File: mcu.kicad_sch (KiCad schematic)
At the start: 0 parts

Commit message: add mcu, sensor, sensor inst, power
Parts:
- added C7: 100n, Capacitor_SMD:C_0805_2012Metric, symbol Device:C
- added H1, H2, H3: MountingHole, MountingHole:MountingHole_3mm, symbol Mechanical:MountingHole
- added Q1, Q2: S8050, Package_TO_SOT_SMD:SOT-23, symbol Transistor_BJT:S8050
- added R8, R9: 12k, Resistor_SMD:R_0805_2012Metric, symbol Device:R
- added U4: ESP32-WROOM-32U, RF_Module:ESP32-WROOM-32U, symbol RF_Module:ESP32-WROOM-32U
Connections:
- new net: Q1.2 (B), R8.2
- new net: Q2.2 (B), R9.2
- new net 3V3: C7.1, U4.2 (VDD)
- new net DTR: Q2.1 (E), R8.1
- new net EN: Q1.3 (C), U4.3 (EN)
- new net GND: C7.2, U4.1 (GND), U4.15 (GND), U4.38 (GND), U4.39 (GND)
- new net IO0: Q2.3 (C), U4.25 (IO0)
- new net RDY: U4.24 (IO2)
- new net RTS: Q1.1 (E), R9.1
- new net RXD: U4.34 (RXD0/IO3)
- new net SCL: U4.36 (IO22)
- new net SDA: U4.33 (IO21)
- new net TXD: U4.35 (TXD0/IO1)

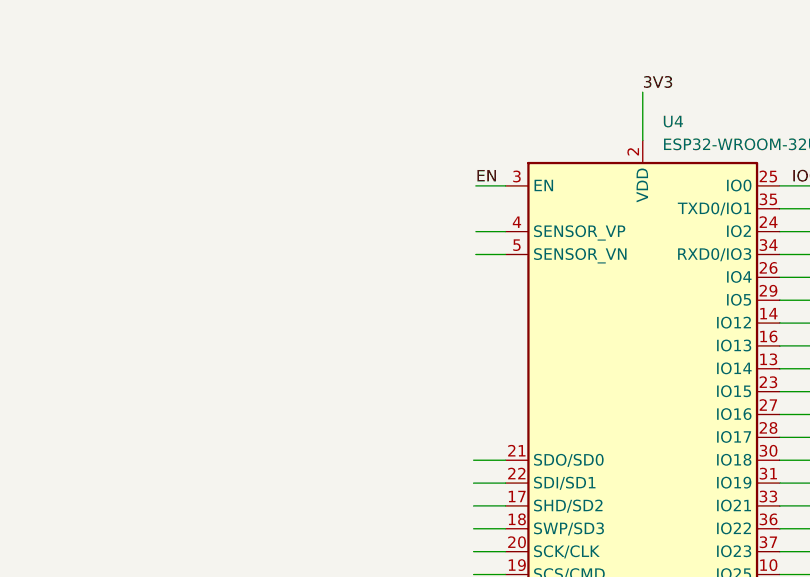
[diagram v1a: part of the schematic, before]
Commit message: add reset button
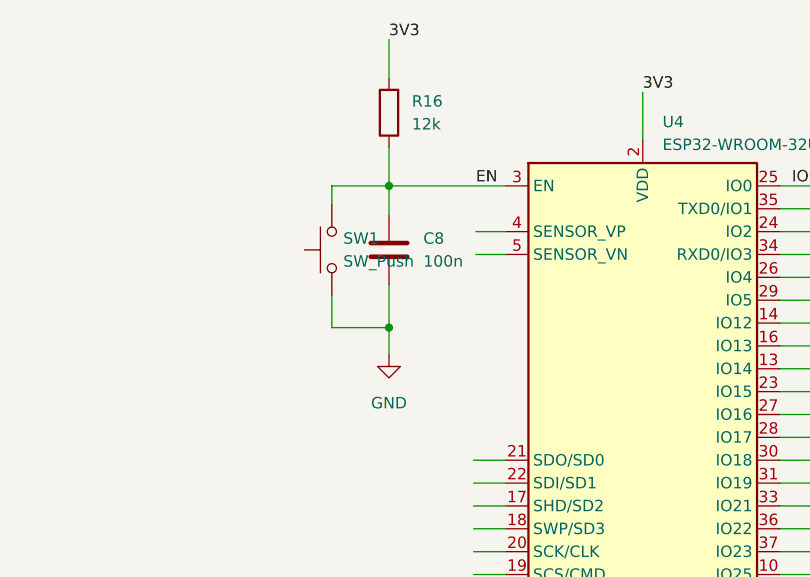
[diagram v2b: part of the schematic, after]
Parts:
- added C8: 100n, Capacitor_SMD:C_0805_2012Metric, symbol Device:C
- added R16: 12k, Resistor_SMD:R_0805_2012Metric, symbol Device:R
- added SW1: SW_Push, symbol Switch:SW_Push
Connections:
- net 3V3: now also R16.2
- net EN: now also C8.1, R16.1, SW1.2
- net GND: now also C8.2, SW1.1
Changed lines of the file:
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@@
   (junction (at 43.18 138.43) (diameter 0) (color 0 0 0 0)
   )
+  (junction (at 113.03 47.498) (diameter 0) (color 0 0 0 0)
+  )
+  (junction (at 113.03 63.246) (diameter 0) (color 0 0 0 0)
+  )
   (junction (at 41.656 155.448) (diameter 0) (color 0 0 0 0)
   )
@@
     (stroke (width 0) (type default))
   )
+  (wire (pts (xy 113.03 47.498) (xy 113.03 50.8))
+    (stroke (width 0) (type default))
+  )
   (wire (pts (xy 156.464 80.518) (xy 160.782 80.518))
     (stroke (width 0) (type default))
@@
     (stroke (width 0) (type default))
   )
+  (wire (pts (xy 113.03 63.246) (xy 113.03 58.42))
+    (stroke (width 0) (type default))
+  )
+  (wire (pts (xy 106.68 63.246) (xy 113.03 63.246))
+    (stroke (width 0) (type default))
+  )
   (wire (pts (xy 156.464 98.298) (xy 160.782 98.298))
     (stroke (width 0) (type default))
@@
     (stroke (width 0) (type default))
   )
+  (wire (pts (xy 113.03 31.242) (xy 113.03 35.56))
+    (stroke (width 0) (type default))
+  )
   (wire (pts (xy 156.464 103.378) (xy 160.782 103.378))
     (stroke (width 0) (type default))
@@
     (stroke (width 0) (type default))
   )
+  (wire (pts (xy 106.68 47.498) (xy 113.03 47.498))
+    (stroke (width 0) (type default))
+  )
   (wire (pts (xy 156.464 67.818) (xy 160.782 67.818))
     (stroke (width 0) (type default))
   )
-  (wire (pts (xy 122.682 47.498) (xy 125.984 47.498))
+  (wire (pts (xy 113.03 47.498) (xy 125.984 47.498))
     (stroke (width 0) (type default))
   )
@@
     (stroke (width 0) (type default))
   )
+  (wire (pts (xy 113.03 63.246) (xy 113.03 66.294))
+    (stroke (width 0) (type default))
+  )
   (wire (pts (xy 141.224 113.538) (xy 141.224 115.824))
     (stroke (width 0) (type default))
@@
     (stroke (width 0) (type default))
   )
+  (wire (pts (xy 113.03 43.18) (xy 113.03 47.498))
+    (stroke (width 0) (type default))
+  )
+  (wire (pts (xy 106.68 59.69) (xy 106.68 63.246))
+    (stroke (width 0) (type default))
+  )
   (wire (pts (xy 43.18 138.43) (xy 43.18 148.336))
+    (stroke (width 0) (type default))
+  )
+  (wire (pts (xy 106.68 49.53) (xy 106.68 47.498))
     (stroke (width 0) (type default))
   )
@@
   (label "IO0" (at 160.782 47.498 180) (fields_autoplaced)
     (effects (font (size 1.27 1.27)) (justify right bottom))
+  )
+  (label "3V3" (at 113.03 31.242 0) (fields_autoplaced)
+    (effects (font (size 1.27 1.27)) (justify left bottom))
   )
   (label "3V3" (at 59.69 56.896 0) (fields_autoplaced)
@@
         (path "/8f227bf3-f4cf-485c-a746-8377af835d89/10be11e8-d58f-4934-80aa-7bf19d703461"
           (reference "H1") (unit 1)
+        )
+      )
+    )
+  )
+  (symbol (lib_id "power:GND") (at 113.03 66.294 0) (unit 1)
+    (in_bom yes) (on_board yes) (dnp no) (fields_autoplaced)
+    (property "Reference" "#PWR029" (at 113.03 72.644 0)
+      (effects (font (size 1.27 1.27)) hide)
+    )
+    (property "Value" "GND" (at 113.03 71.628 0)
+      (effects (font (size 1.27 1.27)))
+    )
+    (property "Footprint" "" (at 113.03 66.294 0)
+      (effects (font (size 1.27 1.27)) hide)
+    )
+    (property "Datasheet" "" (at 113.03 66.294 0)
+      (effects (font (size 1.27 1.27)) hide)
+    )
+    (pin "1")
+    (instances
+      (project "scale"
+        (path "/8f227bf3-f4cf-485c-a746-8377af835d89/10be11e8-d58f-4934-80aa-7bf19d703461"
+          (reference "#PWR029") (unit 1)
+        )
+      )
+    )
+  )
+  (symbol (lib_id "Device:C") (at 113.03 54.61 0) (unit 1)
+    (in_bom yes) (on_board yes) (dnp no) (fields_autoplaced)
+    (property "Reference" "C8" (at 116.84 53.34 0)
+      (effects (font (size 1.27 1.27)) (justify left))
+    )
+    (property "Value" "100n" (at 116.84 55.88 0)
+      (effects (font (size 1.27 1.27)) (justify left))
+    )
+    (property "Footprint" "Capacitor_SMD:C_0805_2012Metric" (at 113.9952 58.42 0)
+      (effects (font (size 1.27 1.27)) hide)
+    )
+    (property "Datasheet" "~" (at 113.03 54.61 0)
+      (effects (font (size 1.27 1.27)) hide)
+    )
+    (pin "1")
+    (pin "2")
+    (instances
+      (project "scale"
+        (path "/8f227bf3-f4cf-485c-a746-8377af835d89/10be11e8-d58f-4934-80aa-7bf19d703461"
+          (reference "C8") (unit 1)
+        )
+      )
+    )
+  )
+  (symbol (lib_id "Switch:SW_Push") (at 106.68 54.61 90) (unit 1)
+    (in_bom yes) (on_board yes) (dnp no) (fields_autoplaced)
+    (property "Reference" "SW1" (at 107.95 53.34 90)
+      (effects (font (size 1.27 1.27)) (justify right))
+    )
+    (property "Value" "SW_Push" (at 107.95 55.88 90)
+      (effects (font (size 1.27 1.27)) (justify right))
+    )
+    (property "Footprint" "" (at 101.6 54.61 0)
+      (effects (font (size 1.27 1.27)) hide)
+    )
+    (property "Datasheet" "~" (at 101.6 54.61 0)
+      (effects (font (size 1.27 1.27)) hide)
+    )
+    (pin "1")
+    (pin "2")
+    (instances
+      (project "scale"
+        (path "/8f227bf3-f4cf-485c-a746-8377af835d89/10be11e8-d58f-4934-80aa-7bf19d703461"
+          (reference "SW1") (unit 1)
         )
       )
@@
         )
       )
+    )
+  )
+  (symbol (lib_id "Device:R") (at 113.03 39.37 180) (unit 1)
+    (in_bom yes) (on_board yes) (dnp no) (fields_autoplaced)
+    (property "Reference" "R16" (at 115.57 38.1 0)
+      (effects (font (size 1.27 1.27)) (justify right))
+    )
+    (property "Value" "12k" (at 115.57 40.64 0)
+      (effects (font (size 1.27 1.27)) (justify right))
+    )
+    (property "Footprint" "Resistor_SMD:R_0805_2012Metric" (at 114.808 39.37 90)
+      (effects (font (size 1.27 1.27)) hide)
+    )
+    (property "Datasheet" "~" (at 113.03 39.37 0)
+      (effects (font (size 1.27 1.27)) hide)
+    )
+    (pin "1")
+    (pin "2")
+    (instances
+      (project "scale"
+        (path "/8f227bf3-f4cf-485c-a746-8377af835d89/10be11e8-d58f-4934-80aa-7bf19d703461"
+          (reference "R16") (unit 1)
+        )
+      )

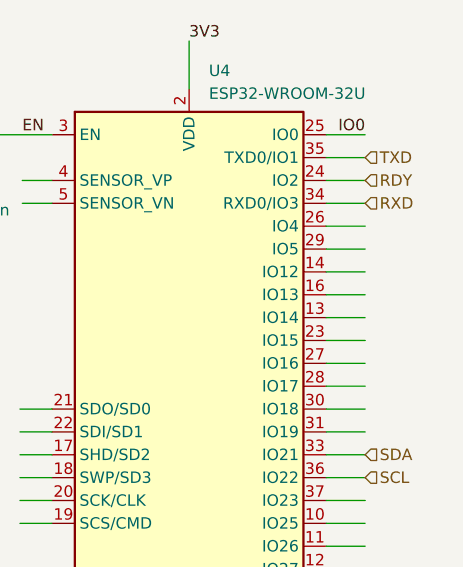
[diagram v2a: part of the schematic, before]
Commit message: add footprint and step
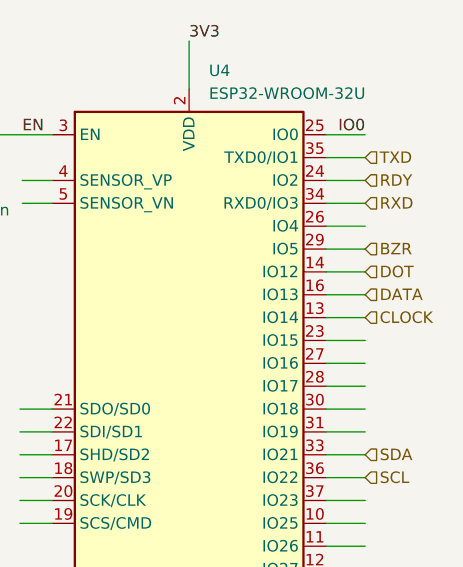
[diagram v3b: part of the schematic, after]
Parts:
- SW1: footprint (none) -> Button_Switch_SMD:SW_DIP_SPSTx01_Slide_6.7x4.1mm_W6.73mm_P2.54mm_LowProfile_JPin
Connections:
- net CLOCK: now reaches U4.13 (IO14)
- net DOT: now reaches U4.14 (IO12)
- net DATA: now reaches U4.16 (IO13)
- net BZR: now reaches U4.29 (IO5)
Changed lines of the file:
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@@
     (effects (font (size 1.27 1.27)) (justify right))
+  )
+  (hierarchical_label "CLOCK" (shape input) (at 160.782 67.818 0) (fields_autoplaced)
+    (effects (font (size 1.27 1.27)) (justify left))
   )
   (hierarchical_label "RDY" (shape input) (at 160.782 52.578 0) (fields_autoplaced)
@@
   (hierarchical_label "RTS" (shape input) (at 37.338 155.448 180) (fields_autoplaced)
     (effects (font (size 1.27 1.27)) (justify right))
+  )
+  (hierarchical_label "BZR" (shape input) (at 160.782 60.198 0) (fields_autoplaced)
+    (effects (font (size 1.27 1.27)) (justify left))
+  )
+  (hierarchical_label "DATA" (shape input) (at 160.782 65.278 0) (fields_autoplaced)
+    (effects (font (size 1.27 1.27)) (justify left))
+  )
+  (hierarchical_label "DOT" (shape input) (at 160.782 62.738 0) (fields_autoplaced)
+    (effects (font (size 1.27 1.27)) (justify left))
   )
   (hierarchical_label "SCL" (shape input) (at 160.782 85.598 0) (fields_autoplaced)
@@
       (effects (font (size 1.27 1.27)) (justify right))
     )
-    (property "Footprint" "" (at 101.6 54.61 0)
-      (effects (font (size 1.27 1.27)) hide)
-    )
+    (property "Footprint" "Button_Switch_SMD:SW_DIP_SPSTx01_Slide_6.7x4.1mm_W6.73mm_P2.54mm_LowProfile_JPin" (at 101.6 54.61 0)
+      (effects (font (size 1.27 1.27)) hide)
+    )

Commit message: update some routings
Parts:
- R16: value 12k -> 10k
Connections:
- net CLOCK: now also U4.12 (IO27); no longer U4.13 (IO14)
- net DATA: now also U4.13 (IO14); no longer U4.16 (IO13)
- net RDY: now also U4.31 (IO19); no longer U4.24 (IO2)
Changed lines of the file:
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@@
     (effects (font (size 1.27 1.27)) (justify right))
   )
-  (hierarchical_label "CLOCK" (shape input) (at 160.782 67.818 0) (fields_autoplaced)
-    (effects (font (size 1.27 1.27)) (justify left))
-  )
-  (hierarchical_label "RDY" (shape input) (at 160.782 52.578 0) (fields_autoplaced)
+  (hierarchical_label "CLOCK" (shape input) (at 160.782 95.758 0) (fields_autoplaced)
+    (effects (font (size 1.27 1.27)) (justify left))
+  )
+  (hierarchical_label "RDY" (shape input) (at 160.782 80.518 0) (fields_autoplaced)
     (effects (font (size 1.27 1.27)) (justify left))
   )
@@
     (effects (font (size 1.27 1.27)) (justify left))
   )
-  (hierarchical_label "DATA" (shape input) (at 160.782 65.278 0) (fields_autoplaced)
+  (hierarchical_label "DATA" (shape input) (at 160.782 67.818 0) (fields_autoplaced)
     (effects (font (size 1.27 1.27)) (justify left))
   )
@@
       (effects (font (size 1.27 1.27)) (justify right))
     )
-    (property "Value" "12k" (at 115.57 40.64 0)
+    (property "Value" "10k" (at 115.57 40.64 0)
       (effects (font (size 1.27 1.27)) (justify right))
     )

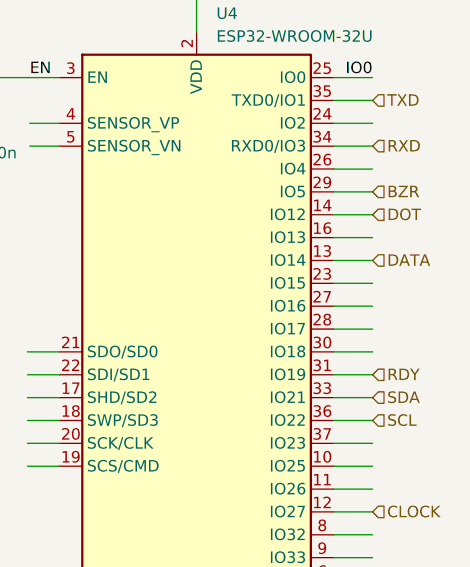
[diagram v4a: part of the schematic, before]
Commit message: change DATA, BZR, and DOT pins
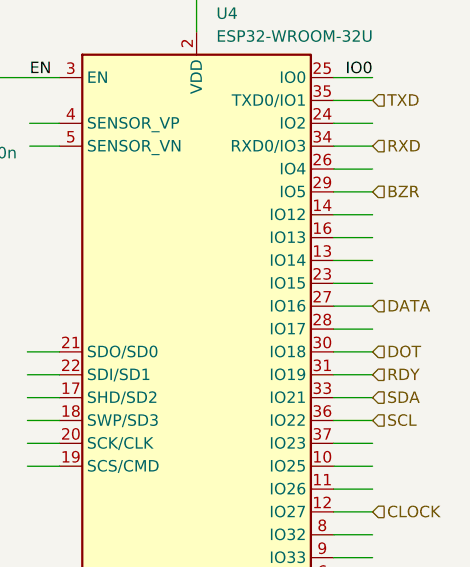
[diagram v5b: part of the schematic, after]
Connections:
- net DATA: now also U4.27 (IO16); no longer U4.13 (IO14)
- net DOT: now also U4.30 (IO18); no longer U4.14 (IO12)
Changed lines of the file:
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@@
     (effects (font (size 1.27 1.27)) (justify left))
   )
-  (hierarchical_label "DATA" (shape input) (at 160.782 67.818 0) (fields_autoplaced)
+  (hierarchical_label "DATA" (shape input) (at 160.782 72.898 0) (fields_autoplaced)
     (effects (font (size 1.27 1.27)) (justify left))
   )
-  (hierarchical_label "DOT" (shape input) (at 160.782 62.738 0) (fields_autoplaced)
+  (hierarchical_label "DOT" (shape input) (at 160.782 77.978 0) (fields_autoplaced)
     (effects (font (size 1.27 1.27)) (justify left))
   )

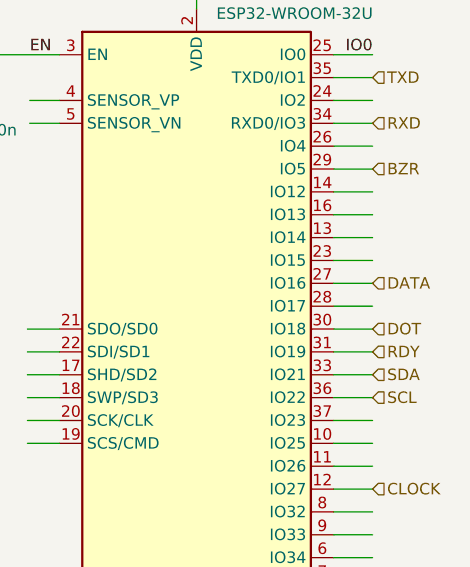
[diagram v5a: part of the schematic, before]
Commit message: change dimensions
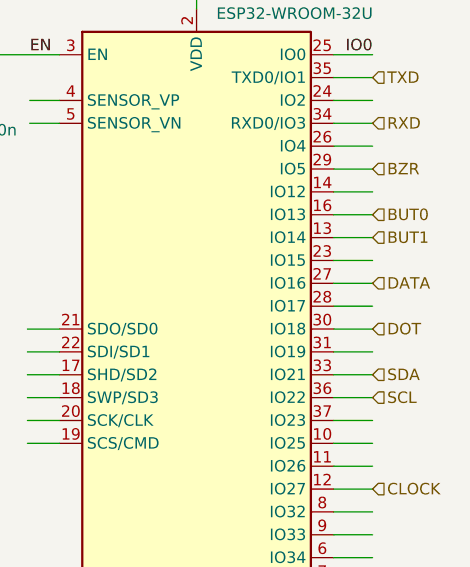
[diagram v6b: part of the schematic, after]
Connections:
- net BUT1: now reaches U4.13 (IO14)
- net BUT0: now reaches U4.16 (IO13)
- net RDY: no longer names the net of U4.31 (IO19)
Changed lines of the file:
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@@
-    (effects (font (size 1.27 1.27)) (justify left))
-  )
-  (hierarchical_label "RDY" (shape input) (at 160.782 80.518 0) (fields_autoplaced)
     (effects (font (size 1.27 1.27)) (justify left))
   )
@@
     (effects (font (size 1.27 1.27)) (justify left))
   )
+  (hierarchical_label "BUT0" (shape input) (at 160.782 65.278 0) (fields_autoplaced)
+    (effects (font (size 1.27 1.27)) (justify left))
+  )
+  (hierarchical_label "BUT1" (shape input) (at 160.782 67.818 0) (fields_autoplaced)
+    (effects (font (size 1.27 1.27)) (justify left))
+  )

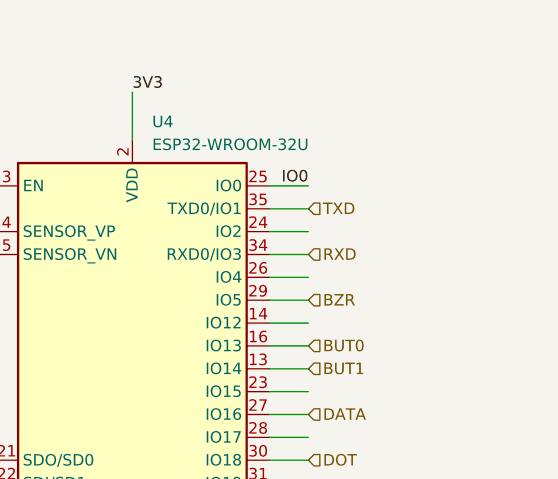
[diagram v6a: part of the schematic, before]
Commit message: add some silkscreen, enable access to BOOT pin
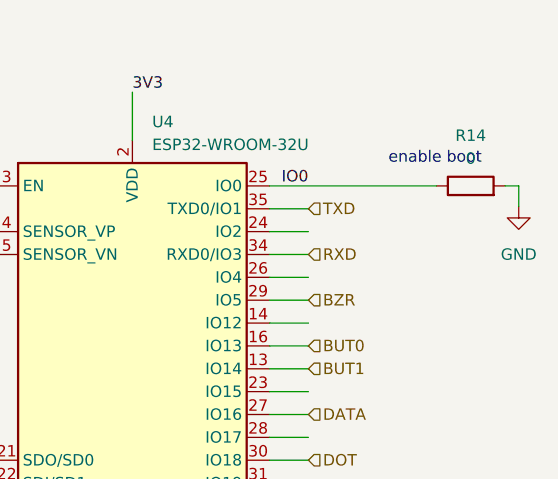
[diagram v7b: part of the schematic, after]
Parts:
- added R14: 0, Resistor_SMD:R_0805_2012Metric, symbol Device:R
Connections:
- net GND: now also R14.2
- net IO0: now also R14.1
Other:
- note added: "enable boot"
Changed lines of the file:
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@@
+    (stroke (width 0) (type default))
+  )
+  (wire (pts (xy 184.15 47.498) (xy 184.15 49.784))
     (stroke (width 0) (type default))
   )
@@
     (stroke (width 0) (type default))
   )
+  (wire (pts (xy 182.626 47.498) (xy 184.15 47.498))
+    (stroke (width 0) (type default))
+  )
   (wire (pts (xy 64.77 163.068) (xy 75.184 163.068))
     (stroke (width 0) (type default))
@@
     (stroke (width 0) (type default))
   )
+  (wire (pts (xy 156.464 47.498) (xy 175.006 47.498))
+    (stroke (width 0) (type default))
+  )
   (wire (pts (xy 59.69 66.04) (xy 59.69 68.834))
     (stroke (width 0) (type default))
   )
-  (wire (pts (xy 156.464 47.498) (xy 160.782 47.498))
-    (stroke (width 0) (type default))
-  )
   (wire (pts (xy 156.464 75.438) (xy 160.782 75.438))
     (stroke (width 0) (type default))
@@
   (wire (pts (xy 156.464 85.598) (xy 160.782 85.598))
     (stroke (width 0) (type default))
+  )
+  (text "enable boot\n" (at 169.672 45.212 0)
+    (effects (font (size 1.27 1.27)) (justify left bottom))
   )
   (label "EN" (at 122.682 47.498 0) (fields_autoplaced)
@@
         (path "/8f227bf3-f4cf-485c-a746-8377af835d89/10be11e8-d58f-4934-80aa-7bf19d703461"
           (reference "SW1") (unit 1)
+        )
+      )
+    )
+  )
+  (symbol (lib_id "Device:R") (at 178.816 47.498 90) (unit 1)
+    (in_bom yes) (on_board yes) (dnp no) (fields_autoplaced)
+    (property "Reference" "R14" (at 178.816 41.91 90)
+      (effects (font (size 1.27 1.27)))
+    )
+    (property "Value" "0" (at 178.816 44.45 90)
+      (effects (font (size 1.27 1.27)))
+    )
+    (property "Footprint" "Resistor_SMD:R_0805_2012Metric" (at 178.816 49.276 90)
+      (effects (font (size 1.27 1.27)) hide)
+    )
+    (property "Datasheet" "~" (at 178.816 47.498 0)
+      (effects (font (size 1.27 1.27)) hide)
+    )
+    (pin "1")
+    (pin "2")
+    (instances
+      (project "scale"
+        (path "/8f227bf3-f4cf-485c-a746-8377af835d89/10be11e8-d58f-4934-80aa-7bf19d703461"
+          (reference "R14") (unit 1)
         )
       )
@@
         )
       )
+    )
+  )
+  (symbol (lib_id "power:GND") (at 184.15 49.784 0) (unit 1)
+    (in_bom yes) (on_board yes) (dnp no) (fields_autoplaced)
+    (property "Reference" "#PWR035" (at 184.15 56.134 0)
+      (effects (font (size 1.27 1.27)) hide)
+    )
+    (property "Value" "GND" (at 184.15 55.118 0)
+      (effects (font (size 1.27 1.27)))
+    )
+    (property "Footprint" "" (at 184.15 49.784 0)
+      (effects (font (size 1.27 1.27)) hide)
+    )
+    (property "Datasheet" "" (at 184.15 49.784 0)
+      (effects (font (size 1.27 1.27)) hide)
+    )
+    (pin "1")
+    (instances
+      (project "scale"
+        (path "/8f227bf3-f4cf-485c-a746-8377af835d89/10be11e8-d58f-4934-80aa-7bf19d703461"
+          (reference "#PWR035") (unit 1)
+        )
+      )
